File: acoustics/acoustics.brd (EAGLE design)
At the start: 76.2 x 101.6 mm, 184 parts, among them U1 ADS124S08IPBSRPBS0032A_L, U2 ADS124S08IPBSRPBS0032A_L, U3 ADS124S08IPBSRPBS0032A_L, U4 ADS124S08IPBSRPBS0032A_L, X1 22-23-2031

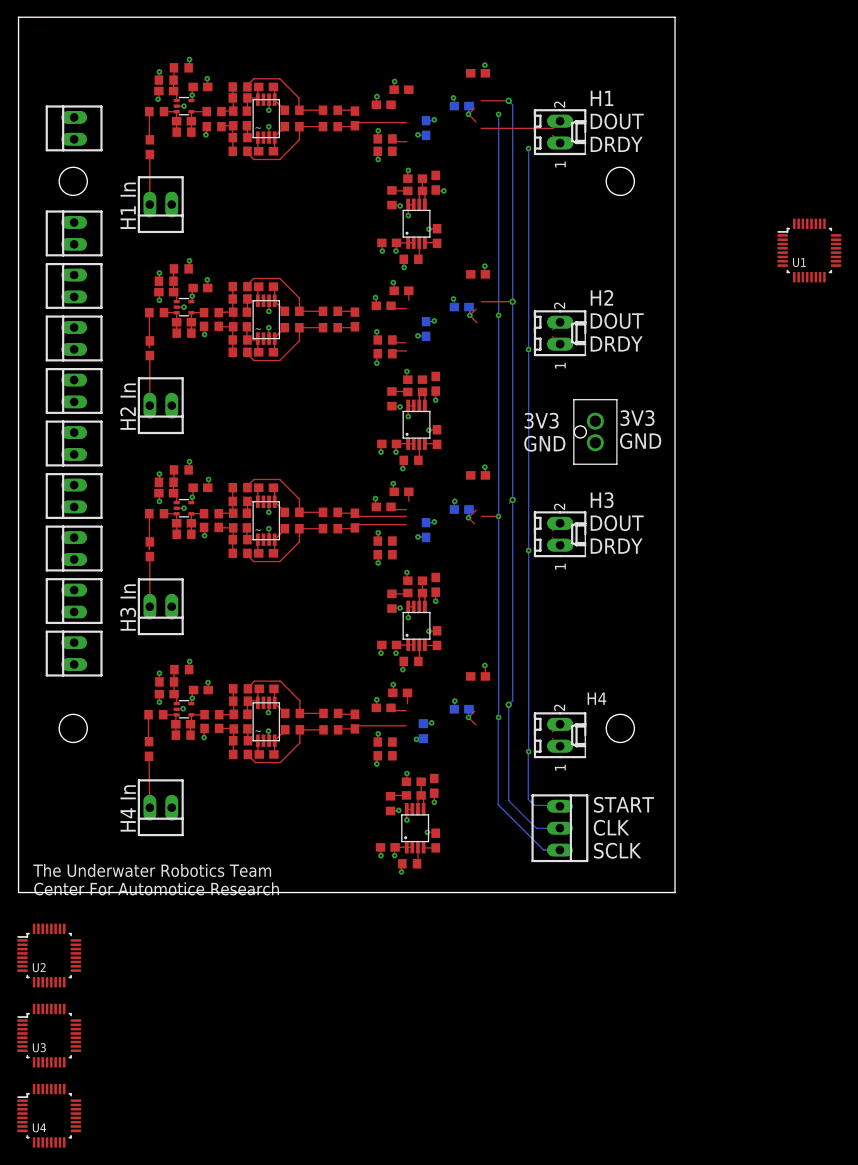
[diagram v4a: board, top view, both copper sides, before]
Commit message: Finished routing ADC
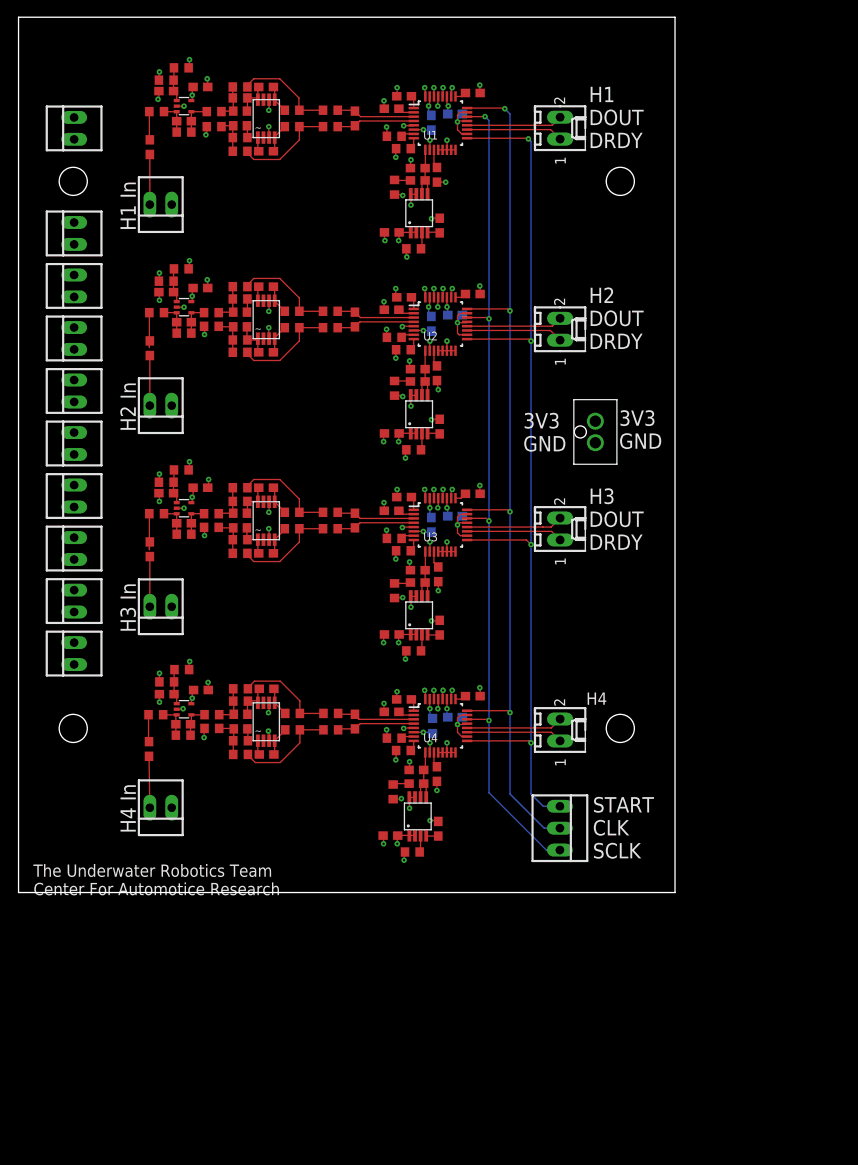
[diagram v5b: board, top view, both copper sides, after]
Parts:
- moved U2 86.2 mm to (74.4, 66.0)
- moved U3 74.7 mm to (74.4, 42.7)
- moved U4 64.1 mm to (74.4, 19.4)
- moved U1 45.3 mm to (74.4, 89.3)
- moved H1ADC_C25 2.37 mm to (78.1, 92.8)
- moved H2_C25 2.37 mm to (78.1, 69.5)
- moved H4_C25 2.37 mm to (78.1, 22.8)
- moved H3_C25 2.22 mm to (78.1, 46.3)
- moved H4_R6 2.22 mm to (70.1, 16.5)
- moved H2_R8 2.18 mm to (70.1, 63.0)
- moved H3_R8 2.18 mm to (70.1, 39.7)
- moved H1ADC_R8 2.16 mm to (70.1, 86.3)
- moved H4RF_C_IN 1.41 mm to (68.6, 6.61)
- moved H4RF_R_0 1.41 mm to (68.9, 11.7)
- moved H4_REFGEN 1.41 mm to (71.7, 8.83)
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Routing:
- net GND: track 92.3 -> 141.9 mm, vias 80 -> 100
- net START: track 80.1 -> 110.0 mm
- net +3V3: track 35.4 -> 57.6 mm, vias 24 -> 36
- net CLK: track 96.3 -> 106.8 mm
- net DOUT_H3: track 1.23 -> 11.3 mm
- net DRDY_H2: track 1.23 -> 11.3 mm
- net DRDY_H1: track 1.22 -> 11.3 mm
- net DRDY_H4: track 1.22 -> 11.2 mm
- net DOUT_H4: track 1.24 -> 11.2 mm
- net DRDY_H3: track 1.23 -> 11.2 mm
- net DOUT_H2: track 1.23 -> 11.2 mm
- net SCLK: track 91.7 -> 99.6 mm
- net ADC4_IN-: track 2.62 -> 9.20 mm
- net ADC1_IN-: track 2.68 -> 9.14 mm
- net ADC2_IN-: track 2.68 -> 9.13 mm
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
